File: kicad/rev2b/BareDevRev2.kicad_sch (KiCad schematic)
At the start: 358 parts, among them J401 TYPE-C-31-M12, Q1 AO3401A, Q301 2N7002, Q302 2N7002, SW301 K2-1187SQ-A4SW-06, U1 BL24C256A-SFRC, U2 JOKER MCU, U201 SGM2007-3.3XN5/TR, U3 USBLC6-2SC6, X1 ARM JTAG, Y1 7325-0800A2010-00

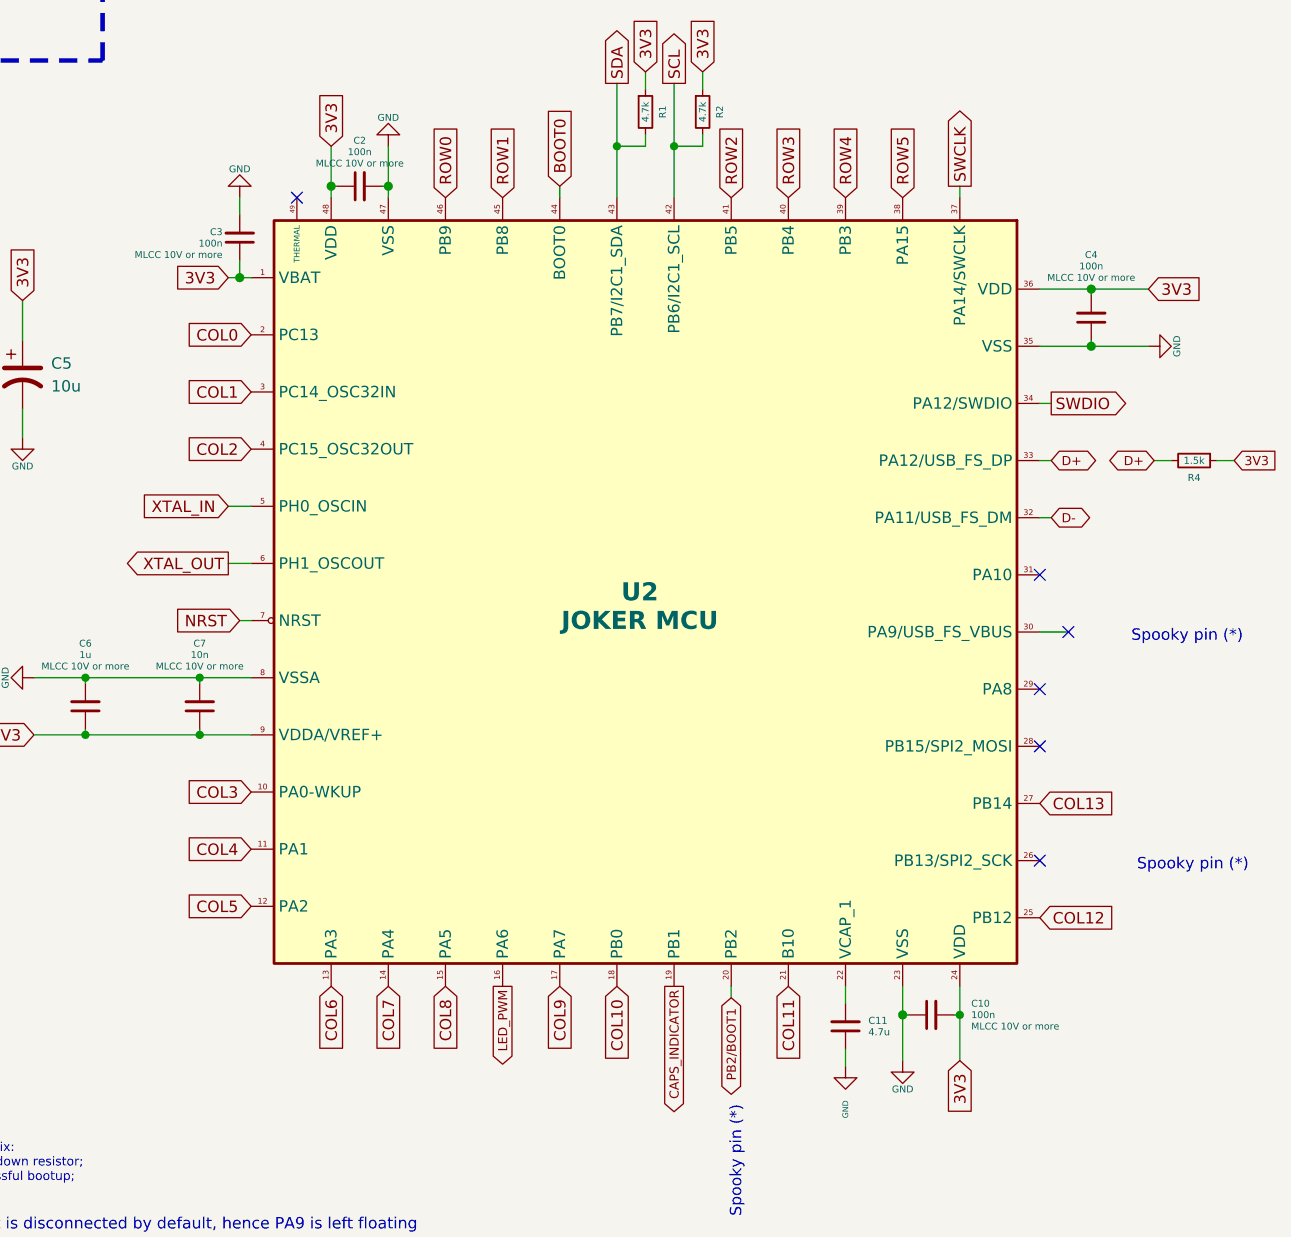
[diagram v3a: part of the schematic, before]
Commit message: rev2b routing done (production files not working with JLCPCB
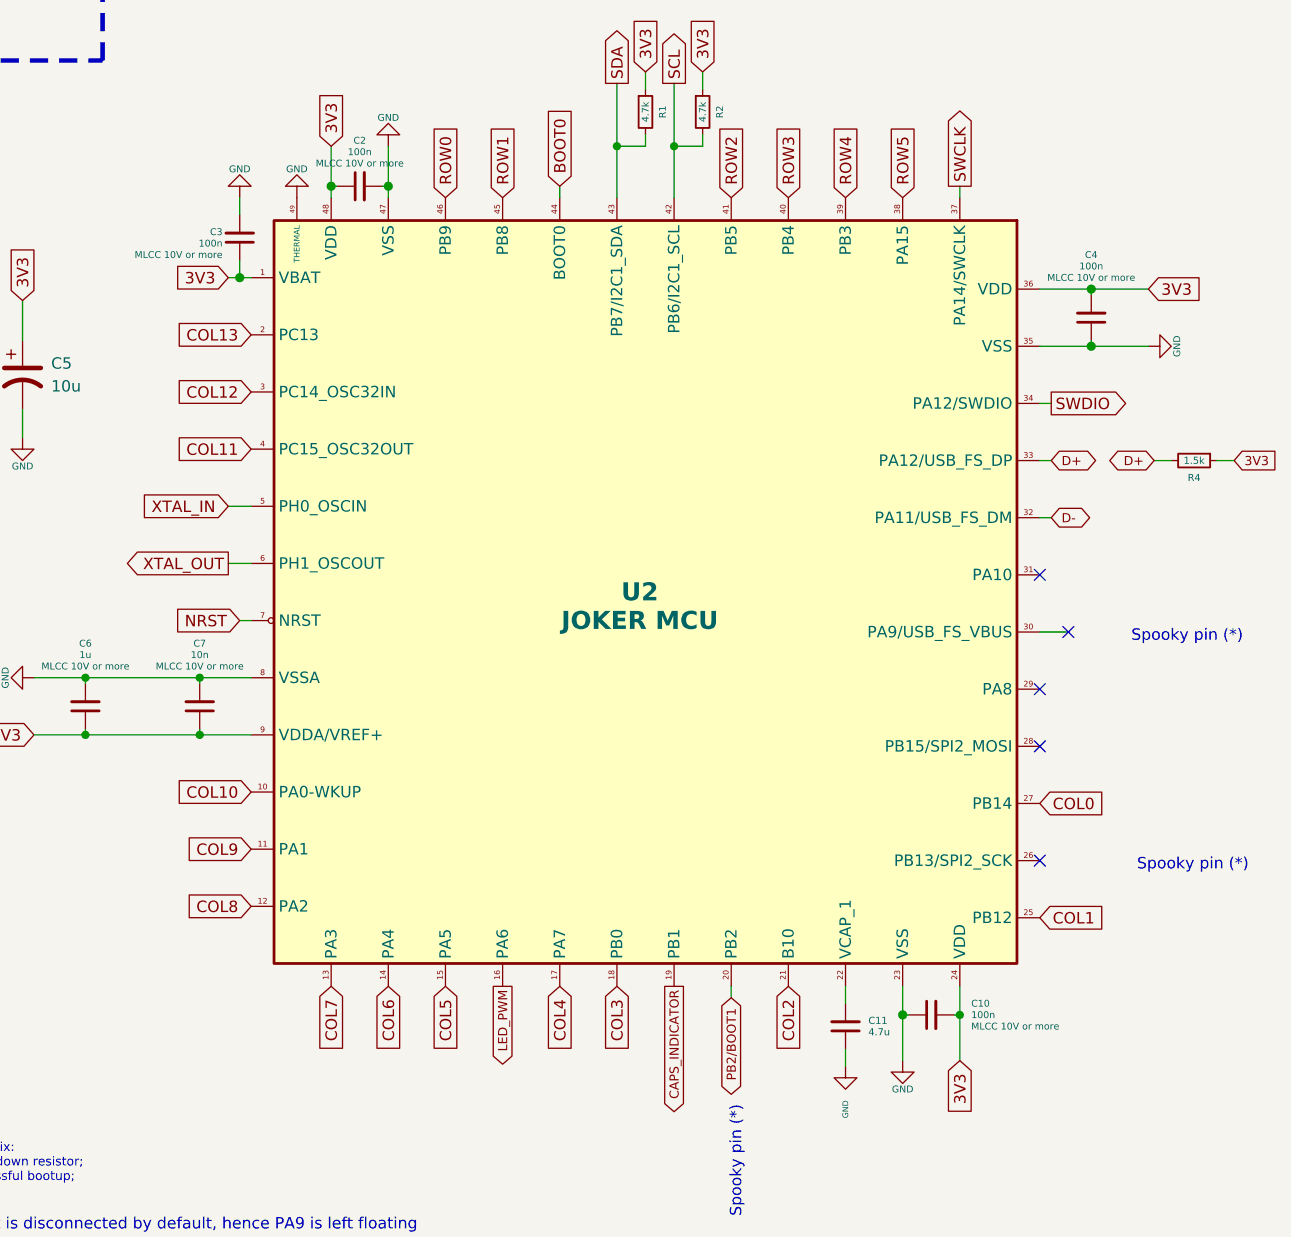
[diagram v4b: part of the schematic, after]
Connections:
- net COL0: now also U2.27 (PB14); no longer U2.2 (PC13)
- net COL1: now also U2.25 (PB12); no longer U2.3 (PC14_OSC32IN)
- net COL10: now also U2.10 (PA0-WKUP); no longer U2.18 (PB0)
- net COL11: now also U2.4 (PC15_OSC32OUT); no longer U2.21 (B10)
- net COL12: now also U2.3 (PC14_OSC32IN); no longer U2.25 (PB12)
- net COL13: now also U2.2 (PC13); no longer U2.27 (PB14)
- net COL2: now also U2.21 (B10); no longer U2.4 (PC15_OSC32OUT)
- net COL3: now also U2.18 (PB0); no longer U2.10 (PA0-WKUP)
- net COL4: now also U2.17 (PA7); no longer U2.11 (PA1)
- net COL5: now also U2.15 (PA5); no longer U2.12 (PA2)
- net COL6: now also U2.14 (PA4); no longer U2.13 (PA3)
- net COL7: now also U2.13 (PA3); no longer U2.14 (PA4)
- net COL8: now also U2.12 (PA2); no longer U2.15 (PA5)
- net COL9: now also U2.11 (PA1); no longer U2.17 (PA7)
- net GND: now also U2.49 (THERMAL)
- no-connect marks 8 -> 7
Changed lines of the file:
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@@
   (no_connect (at 288.925 106.68))
   (no_connect (at 288.925 125.73))
-  (no_connect (at 206.375 52.07))
   (no_connect (at 53.975 127.635))
   (no_connect (at 288.925 113.03))
@@
     )
   )
-  (global_label "COL11" (shape input) (at 260.985 139.7 270) (fields_autoplaced)
+  (global_label "COL2" (shape input) (at 260.985 139.7 270) (fields_autoplaced)
     (effects (font (size 1.27 1.27)) (justify right))
-    (property "Intersheet References" "${INTERSHEET_REFS}" (id 0) (at 260.9056 148.3512 90)
+    (property "Intersheet References" "${INTERSHEET_REFS}" (id 0) (at 260.9056 147.1417 90)
       (effects (font (size 1.27 1.27)) (justify right) hide)
     )
@@
     )
   )
-  (global_label "COL5" (shape input) (at 201.295 130.81 180) (fields_autoplaced)
+  (global_label "COL8" (shape input) (at 201.295 130.81 180) (fields_autoplaced)
     (effects (font (size 1.27 1.27)) (justify right))
     (property "Intersheet References" "${INTERSHEET_REFS}" (id 0) (at 193.8533 130.7306 0)
@@
     )
   )
-  (global_label "COL8" (shape input) (at 222.885 139.7 270) (fields_autoplaced)
+  (global_label "COL5" (shape input) (at 222.885 139.7 270) (fields_autoplaced)
     (effects (font (size 1.27 1.27)) (justify right))
     (property "Intersheet References" "${INTERSHEET_REFS}" (id 0) (at 222.8056 147.1417 90)
@@
     )
   )
-  (global_label "COL13" (shape input) (at 288.925 119.38 0) (fields_autoplaced)
+  (global_label "COL0" (shape input) (at 288.925 119.38 0) (fields_autoplaced)
     (effects (font (size 1.27 1.27)) (justify left))
-    (property "Intersheet References" "${INTERSHEET_REFS}" (id 0) (at 297.5762 119.3006 0)
+    (property "Intersheet References" "${INTERSHEET_REFS}" (id 0) (at 296.3667 119.3006 0)
       (effects (font (size 1.27 1.27)) (justify left) hide)
     )
   )
-  (global_label "COL12" (shape input) (at 288.925 132.08 0) (fields_autoplaced)
+  (global_label "COL1" (shape input) (at 288.925 132.08 0) (fields_autoplaced)
     (effects (font (size 1.27 1.27)) (justify left))
-    (property "Intersheet References" "${INTERSHEET_REFS}" (id 0) (at 297.5762 132.0006 0)
+    (property "Intersheet References" "${INTERSHEET_REFS}" (id 0) (at 296.3667 132.0006 0)
       (effects (font (size 1.27 1.27)) (justify left) hide)
     )
@@
     )
   )
-  (global_label "COL4" (shape input) (at 201.295 124.46 180) (fields_autoplaced)
+  (global_label "COL9" (shape input) (at 201.295 124.46 180) (fields_autoplaced)
     (effects (font (size 1.27 1.27)) (justify right))
     (property "Intersheet References" "${INTERSHEET_REFS}" (id 0) (at 193.8533 124.3806 0)
@@
     )
   )
-  (global_label "COL3" (shape input) (at 201.295 118.11 180) (fields_autoplaced)
+  (global_label "COL10" (shape input) (at 201.295 118.11 180) (fields_autoplaced)
     (effects (font (size 1.27 1.27)) (justify right))
-    (property "Intersheet References" "${INTERSHEET_REFS}" (id 0) (at 193.8533 118.0306 0)
+    (property "Intersheet References" "${INTERSHEET_REFS}" (id 0) (at 192.6438 118.0306 0)
       (effects (font (size 1.27 1.27)) (justify right) hide)
     )
@@
     )
   )
-  (global_label "COL9" (shape input) (at 235.585 139.7 270) (fields_autoplaced)
+  (global_label "COL4" (shape input) (at 235.585 139.7 270) (fields_autoplaced)
     (effects (font (size 1.27 1.27)) (justify right))
     (property "Intersheet References" "${INTERSHEET_REFS}" (id 0) (at 235.5056 147.1417 90)
@@
     )
   )
-  (global_label "COL1" (shape input) (at 201.295 73.66 180) (fields_autoplaced)
+  (global_label "COL12" (shape input) (at 201.295 73.66 180) (fields_autoplaced)
     (effects (font (size 1.27 1.27)) (justify right))
-    (property "Intersheet References" "${INTERSHEET_REFS}" (id 0) (at 193.8533 73.5806 0)
+    (property "Intersheet References" "${INTERSHEET_REFS}" (id 0) (at 192.6438 73.5806 0)
       (effects (font (size 1.27 1.27)) (justify right) hide)
     )
@@
     )
   )
-  (global_label "COL10" (shape input) (at 241.935 139.7 270) (fields_autoplaced)
+  (global_label "COL3" (shape input) (at 241.935 139.7 270) (fields_autoplaced)
     (effects (font (size 1.27 1.27)) (justify right))
-    (property "Intersheet References" "${INTERSHEET_REFS}" (id 0) (at 241.8556 148.3512 90)
+    (property "Intersheet References" "${INTERSHEET_REFS}" (id 0) (at 241.8556 147.1417 90)
       (effects (font (size 1.27 1.27)) (justify right) hide)
     )
   )
-  (global_label "COL7" (shape input) (at 216.535 139.7 270) (fields_autoplaced)
+  (global_label "COL6" (shape input) (at 216.535 139.7 270) (fields_autoplaced)
     (effects (font (size 1.27 1.27)) (justify right))
     (property "Intersheet References" "${INTERSHEET_REFS}" (id 0) (at 216.4556 147.1417 90)
@@
     )
   )
-  (global_label "COL6" (shape input) (at 210.185 139.7 270) (fields_autoplaced)
+  (global_label "COL7" (shape input) (at 210.185 139.7 270) (fields_autoplaced)
     (effects (font (size 1.27 1.27)) (justify right))
     (property "Intersheet References" "${INTERSHEET_REFS}" (id 0) (at 210.1056 147.1417 90)
@@
     )
   )
-  (global_label "COL2" (shape input) (at 201.295 80.01 180) (fields_autoplaced)
+  (global_label "COL11" (shape input) (at 201.295 80.01 180) (fields_autoplaced)
     (effects (font (size 1.27 1.27)) (justify right))
-    (property "Intersheet References" "${INTERSHEET_REFS}" (id 0) (at 193.8533 79.9306 0)
+    (property "Intersheet References" "${INTERSHEET_REFS}" (id 0) (at 192.6438 79.9306 0)
       (effects (font (size 1.27 1.27)) (justify right) hide)
     )
@@
     )
   )
-  (global_label "COL0" (shape input) (at 201.295 67.31 180) (fields_autoplaced)
+  (global_label "COL13" (shape input) (at 201.295 67.31 180) (fields_autoplaced)
     (effects (font (size 1.27 1.27)) (justify right))
-    (property "Intersheet References" "${INTERSHEET_REFS}" (id 0) (at 193.8533 67.2306 0)
+    (property "Intersheet References" "${INTERSHEET_REFS}" (id 0) (at 192.6438 67.2306 0)
       (effects (font (size 1.27 1.27)) (justify right) hide)
     )
@@
     (pin "2")
   )
+  (symbol (lib_id "power:GND") (at 206.375 52.07 180) (unit 1)
+    (in_bom yes) (on_board yes)
+    (property "Reference" "#PWR?" (id 0) (at 206.375 45.72 0)
+      (effects (font (size 1.27 1.27)) hide)
+    )
+    (property "Value" "GND" (id 1) (at 206.375 48.895 0)
+      (effects (font (size 0.762 0.762)))
+    )
+    (property "Footprint" "" (id 2) (at 206.375 52.07 0)
+      (effects (font (size 1.27 1.27)) hide)
+    )
+    (property "Datasheet" "" (id 3) (at 206.375 52.07 0)
+      (effects (font (size 1.27 1.27)) hide)
+    )
+    (pin "1")
+  )
   (symbol (lib_id "acheron_Symbols:Mechanical_Switch") (at 48.895 260.35 0) (unit 1)
     (in_bom yes) (on_board yes)
@@
       (reference "#PWR0407") (unit 1) (value "GND") (footprint "")
     )
+    (path "/af52043d-b83f-4206-88fd-0af042ec73e3"
+      (reference "#PWR?") (unit 1) (value "GND") (footprint "")
+    )
     (path "/dea96ffa-f040-44f2-9288-2280878ceaa6"
